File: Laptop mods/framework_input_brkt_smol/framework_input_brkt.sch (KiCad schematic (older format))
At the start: 7 parts, among them J1 FPR_LED, J2 input_conn, J3 PWRSW, J4 USB, J6 KBL

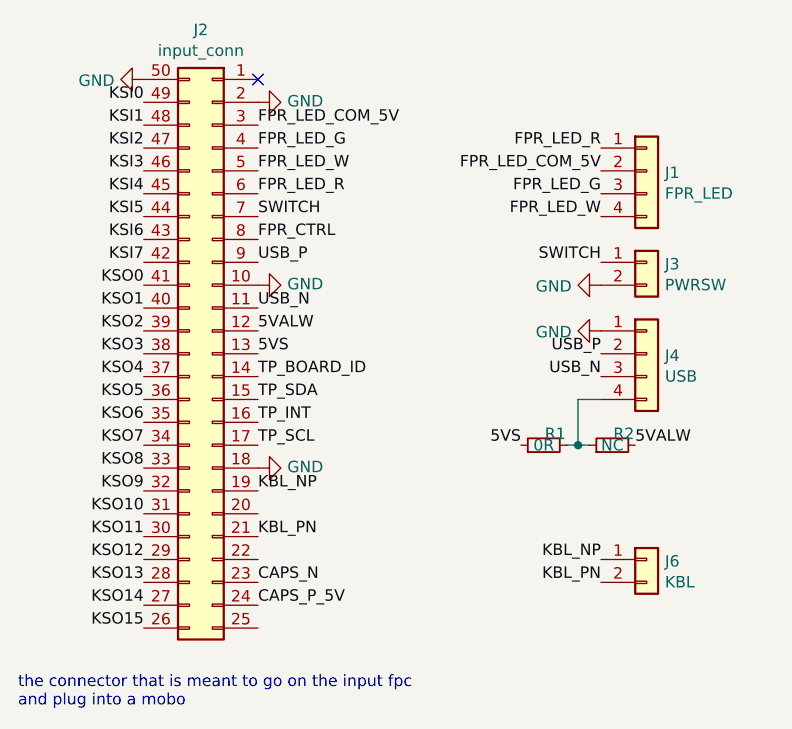
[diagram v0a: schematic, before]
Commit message: framework_input_brkt_smol: adding resistor to RGW LED, adding Amphenol connector STEP, changing on-board PCB name
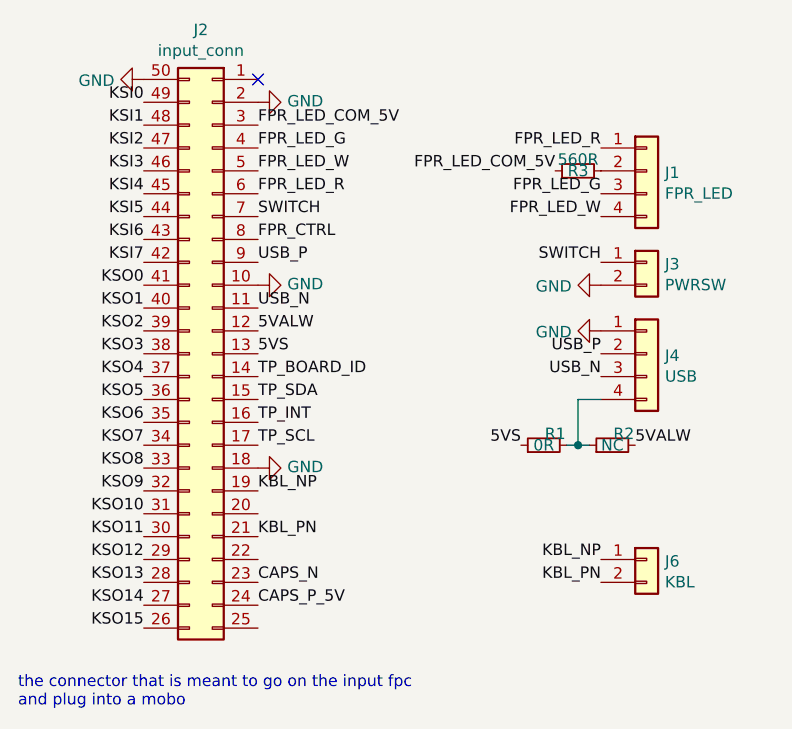
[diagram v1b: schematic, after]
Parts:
- added R3: 560R, Resistor_SMD:R_0603_1608Metric, symbol Device:R_Small
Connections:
- net FPR_LED_COM_5V: now also R3.1; no longer J1.2 (Pin_2)
- new net: J1.2 (Pin_2), R3.2
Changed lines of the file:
@@
 Text Label 8250 3050 2    50   ~ 0
 FPR_LED_G
-Text Label 8250 2950 2    50   ~ 0
+Text Label 8050 2950 2    50   ~ 0
 FPR_LED_COM_5V
 $Comp
@@
 Wire Wire Line
 	8150 4150 8200 4150
+$Comp
+L Device:R_Small R3
+U 1 1 627BC9BD
+P 8150 2950
+F 0 "R3" V 8150 2950 50  0000 C CNN
+F 1 "560R" V 8200 2950 50  0000 C CNN
+F 2 "Resistor_SMD:R_0603_1608Metric" H 8150 2950 50  0001 C CNN
+F 3 "~" H 8150 2950 50  0001 C CNN
+	1    8150 2950
+	0    -1   -1   0
+$EndComp
 $EndSCHEMATC

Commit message: framework_input_brkt_smol: v2, fixed the critical pinout error and rerouted the board; added the caps lock LED connections
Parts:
- removed J2: input_conn, framework_input_brkt:Amphenol_10156001, symbol Connector_Generic:Conn_02x25_Counter_Clockwise
- removed J6: KBL, Connector_PinHeader_2.00mm:PinHeader_1x02_P2.00mm_Vertical, symbol Connector_Generic:Conn_01x02
- added J2: fpc_input_conn, framework_input_brkt:Amphenol_10156001, symbol frmw_conn:fpc_input_conn
- added J5: KnC, Connector_PinHeader_2.00mm:PinHeader_1x04_P2.00mm_Vertical, symbol Connector_Generic:Conn_01x04
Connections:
- net labels added: KBL_P
- net labels removed: KBL_NP, KBL_PN
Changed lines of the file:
@@
 Text Label 6750 3650 0    50   ~ 0
 5VALW
-$Comp
-L Connector_Generic:Conn_02x25_Counter_Clockwise J2
-U 1 1 627884F8
-P 6550 3750
-F 0 "J2" H 6600 5167 50  0000 C CNN
-F 1 "input_conn" H 6600 5076 50  0000 C CNN
-F 2 "framework_input_brkt:Amphenol_10156001" H 6550 3750 50  0001 C CNN
-F 3 "~" H 6550 3750 50  0001 C CNN
-	1    6550 3750
-	-1   0    0    -1
-$EndComp
-$Comp
-L Connector_Generic:Conn_01x02 J3
-U 1 1 62794A5A
-P 8450 3350
-F 0 "J3" H 8530 3342 50  0000 L CNN
-F 1 "PWRSW" H 8530 3251 50  0000 L CNN
-F 2 "Connector_PinHeader_2.54mm:PinHeader_1x02_P2.54mm_Vertical" H 8450 3350 50  0001 C CNN
-F 3 "~" H 8450 3350 50  0001 C CNN
-	1    8450 3350
-	1    0    0    -1
-$EndComp
 Text Label 8250 3350 2    50   ~ 0
 SWITCH
@@
 	0    1    1    0
 $EndComp
-$Comp
-L Connector_Generic:Conn_01x02 J6
-U 1 1 627B74CA
-P 8450 4650
-F 0 "J6" H 8530 4642 50  0000 L CNN
-F 1 "KBL" H 8530 4551 50  0000 L CNN
-F 2 "Connector_PinHeader_2.00mm:PinHeader_1x02_P2.00mm_Vertical" H 8450 4650 50  0001 C CNN
-F 3 "~" H 8450 4650 50  0001 C CNN
-	1    8450 4650
-	1    0    0    -1
-$EndComp
 Text Notes 5700 5300 0    50   ~ 0
 the connector that is meant to go on the input fpc\nand plug into a mobo
@@
 $EndComp
 Text Label 6750 4350 0    50   ~ 0
-KBL_NP
+KBL_P
 Text Label 6750 4550 0    50   ~ 0
-KBL_PN
-Text Label 8250 4650 2    50   ~ 0
-KBL_NP
-Text Label 8250 4750 2    50   ~ 0
-KBL_PN
+KBL_P
 Wire Wire Line
 	8100 4150 8150 4150
@@
 	0    -1   -1   0
 $EndComp
+$Comp
+L frmw_conn:fpc_input_conn J2
+U 1 1 6285596B
+P 6450 3750
+F 0 "J2" H 6500 5167 50  0000 C CNN
+F 1 "fpc_input_conn" H 6500 5076 50  0000 C CNN
+F 2 "framework_input_brkt:Amphenol_10156001" H 6450 3750 50  0001 C CNN
+F 3 "~" H 6450 3750 50  0001 C CNN
+	1    6450 3750
+	1    0    0    -1
+$EndComp
+Text Label 8550 5150 2    50   ~ 0
+CAPS_N
+Text Label 8550 5050 2    50   ~ 0
+KBL_P
+$Comp
+L power:GND #PWR0101
+U 1 1 6286BD9B
+P 6750 4450
+F 0 "#PWR0101" H 6750 4200 50  0001 C CNN
+F 1 "GND" V 6755 4322 50  0000 R CNN
+F 2 "" H 6750 4450 50  0001 C CNN
+F 3 "" H 6750 4450 50  0001 C CNN
+	1    6750 4450
+	0    -1   -1   0
+$EndComp
+$Comp
+L power:GND #PWR0102
+U 1 1 6286CA6E
+P 6750 4650
+F 0 "#PWR0102" H 6750 4400 50  0001 C CNN
+F 1 "GND" V 6755 4522 50  0000 R CNN
+F 2 "" H 6750 4650 50  0001 C CNN
+F 3 "" H 6750 4650 50  0001 C CNN
+	1    6750 4650
+	0    -1   -1   0
+$EndComp
+$Comp
+L power:GND #PWR0103
+U 1 1 6286CDB6
+P 6750 4950
+F 0 "#PWR0103" H 6750 4700 50  0001 C CNN
+F 1 "GND" V 6755 4822 50  0000 R CNN
+F 2 "" H 6750 4950 50  0001 C CNN
+F 3 "" H 6750 4950 50  0001 C CNN
+	1    6750 4950
+	0    -1   -1   0
+$EndComp
+$Comp
+L Connector_Generic:Conn_01x04 J5
+U 1 1 62875384
+P 8750 5050
+F 0 "J5" H 8830 5042 50  0000 L CNN
+F 1 "KnC" H 8830 4951 50  0000 L CNN
+F 2 "Connector_PinHeader_2.00mm:PinHeader_1x04_P2.00mm_Vertical" H 8750 5050 50  0001 C CNN
+F 3 "~" H 8750 5050 50  0001 C CNN
+	1    8750 5050
+	1    0    0    -1
+$EndComp
+$Comp
+L power:GND #PWR0104
+U 1 1 62879DE0
+P 8550 4950
+F 0 "#PWR0104" H 8550 4700 50  0001 C CNN
+F 1 "GND" V 8500 4800 50  0000 R CNN
+F 2 "" H 8550 4950 50  0001 C CNN
+F 3 "" H 8550 4950 50  0001 C CNN
+	1    8550 4950
+	0    1    1    0
+$EndComp
+Text Label 8550 5250 2    50   ~ 0
+CAPS_P_5V
+$Comp
+L Connector_Generic:Conn_01x02 J3
+U 1 1 62794A5A
+P 8450 3450
+F 0 "J3" H 8530 3442 50  0000 L CNN
+F 1 "PWRSW" H 8530 3351 50  0000 L CNN
+F 2 "Connector_PinHeader_2.54mm:PinHeader_1x02_P2.54mm_Vertical" H 8450 3450 50  0001 C CNN
+F 3 "~" H 8450 3450 50  0001 C CNN
+	1    8450 3450
+	1    0    0    1
+$EndComp
 $EndSCHEMATC
